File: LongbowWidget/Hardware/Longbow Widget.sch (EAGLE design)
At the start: 29 parts, among them J0 CONN_6SCREW_2.54, J1 CONN_6SCREW_2.54, Q2 DMG3404, U1 TPS7A0533DBV, U2 SN65HVD33RHL

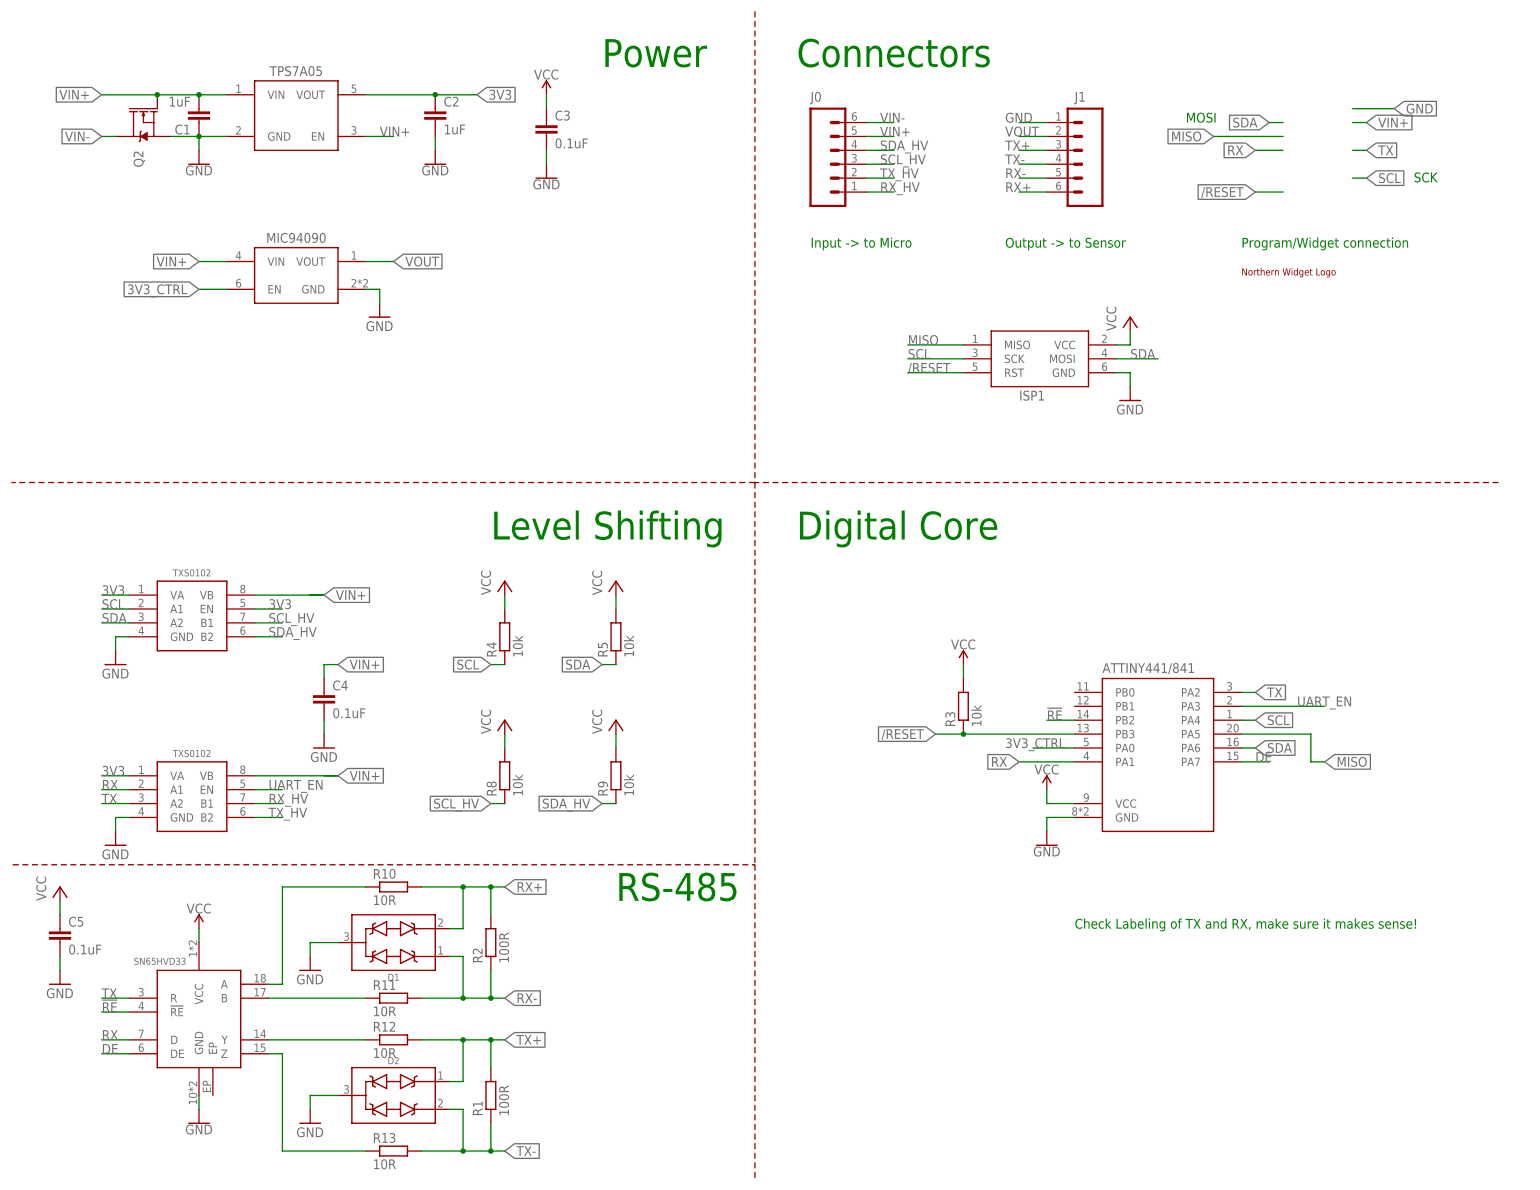
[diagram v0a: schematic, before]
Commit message: Updated to v0.3
Minor update, added jumpers to allow for conversion to 2 wire RS485 without external jumping/connection. Made edits in Eagle, generated new gerber files and updated BoM to reflect "jumper" parts
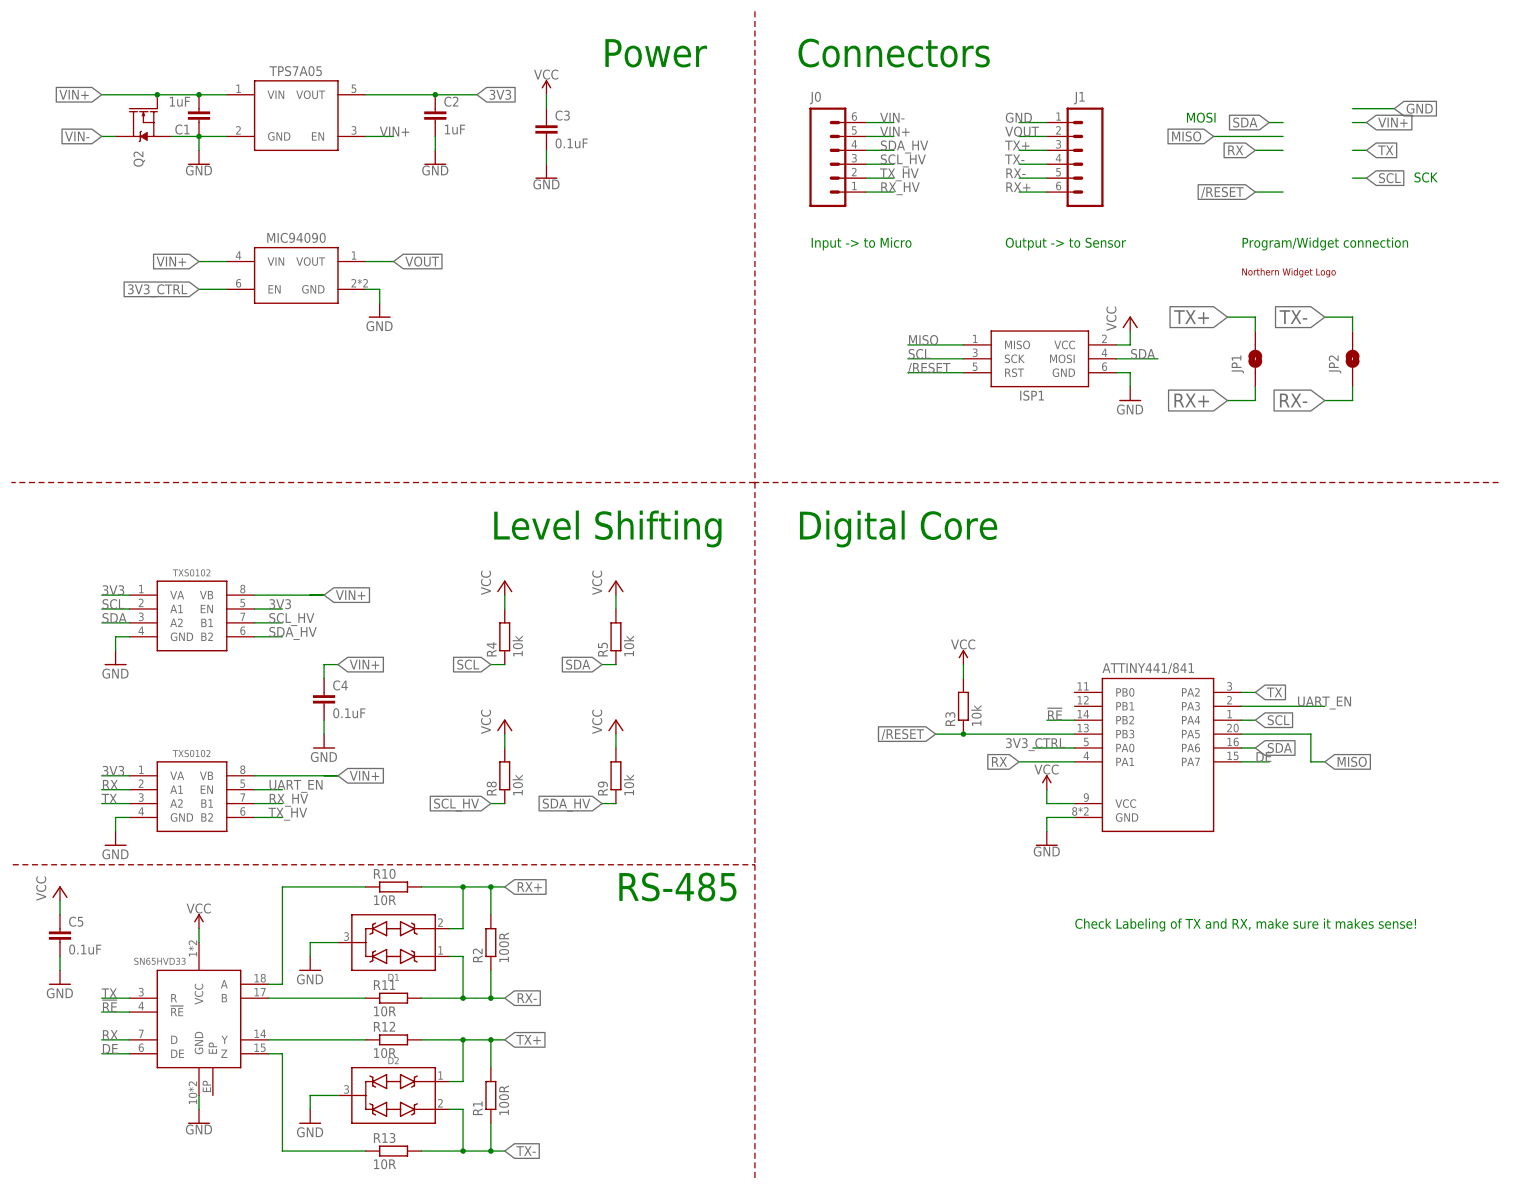
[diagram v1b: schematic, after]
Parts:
- added JP1, JP2: JUMPER-SMT_2_NO_SILK, SparkFun-Jumpers:JUMPER-SMT_2_NO_SILK
- U1: DIGIKEY (none) -> 296-TPS7A0533PDBVRCT-ND
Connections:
- net RX+: now also JP1.1
- net RX-: now also JP2.1
- net TX+: now also JP1.2
- net TX-: now also JP2.2

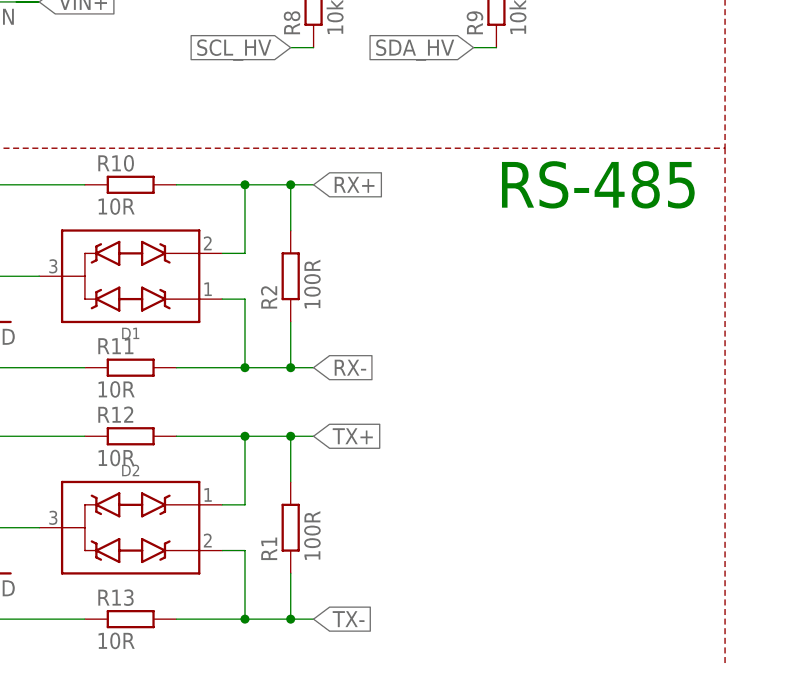
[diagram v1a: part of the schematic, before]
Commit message: Added A and B value note in schematic
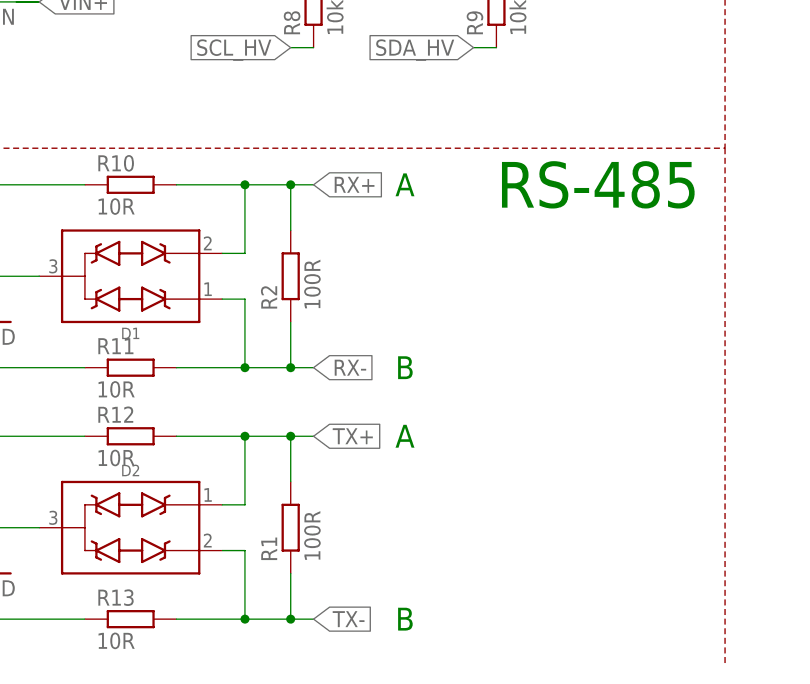
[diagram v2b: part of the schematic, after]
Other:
- note added: "A"
- note added: "B"
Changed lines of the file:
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@@
 <?xml version="1.0" encoding="utf-8"?>
 <!DOCTYPE eagle SYSTEM "eagle.dtd">
-<eagle version="9.5.2">
+<eagle version="9.4.2">
 <drawing>
 <settings>
@@
 <text x="185.42" y="170.18" size="1.778" layer="91">Output -&gt; to Sensor</text>
 <text x="228.6" y="170.18" size="1.778" layer="91">Program/Widget connection</text>
+<text x="104.14" y="5.08" size="2.54" layer="91" align="center">B</text>
+<text x="104.14" y="33.02" size="2.54" layer="91" align="center">B</text>
+<text x="104.14" y="53.34" size="2.54" layer="91" align="center">A</text>
+<text x="104.14" y="25.4" size="2.54" layer="91" align="center">A</text>
 </plain>
 <instances>
